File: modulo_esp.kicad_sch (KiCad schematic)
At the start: 0 parts

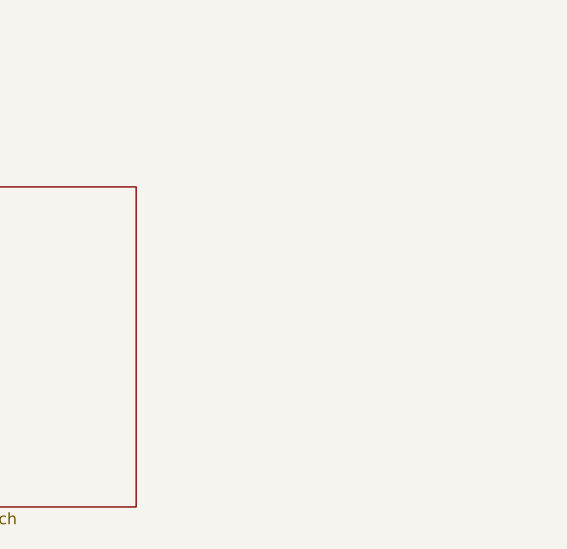
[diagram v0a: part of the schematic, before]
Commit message: Adicionado BG95-M3 e TVS do PHY Ethernet
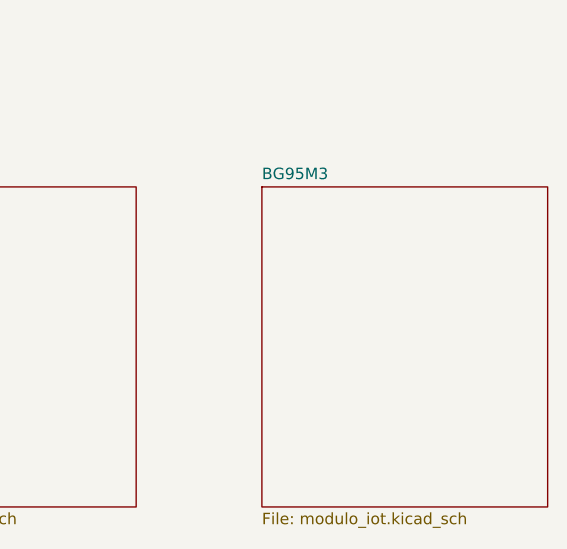
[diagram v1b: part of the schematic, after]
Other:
- added sheet BG95M3 (modulo_iot.kicad_sch)
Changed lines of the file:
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@@
+    )
+  )
+  (sheet (at 144.78 100.33) (size 31.75 35.56) (fields_autoplaced)
+    (stroke (width 0.1524) (type solid) (color 0 0 0 0))
+    (fill (color 0 0 0 0.0000))
+    (property "Sheet name" "BG95M3" (id 0) (at 144.78 99.6184 0)
+      (effects (font (size 1.27 1.27)) (justify left bottom))
+    )
+    (property "Sheet file" "modulo_iot.kicad_sch" (id 1) (at 144.78 136.4746 0)
+      (effects (font (size 1.27 1.27)) (justify left top))
     )
   )
@@
     (path "/7b11f4fb-9ca5-474d-979f-5c95c69d797c" (page "3"))
     (path "/fad468d2-9036-4024-8b69-088056b4a2a2" (page "4"))
+    (path "/42a2b2c3-5ebb-49d9-aedb-3a59eff4693b" (page "5"))
   )
   (symbol_instances
@@
       (reference "#PWR061") (unit 1) (value "GNDREF") (footprint "")
     )
+    (path "/42a2b2c3-5ebb-49d9-aedb-3a59eff4693b/17eac0f3-7baf-4b59-a491-3c654eaf5fe4"
+      (reference "#PWR?") (unit 1) (value "+3.3V") (footprint "")
+    )
+    (path "/42a2b2c3-5ebb-49d9-aedb-3a59eff4693b/60039f13-a1c0-40c4-8050-5e51646e9a0d"
+      (reference "#PWR?") (unit 1) (value "GNDREF") (footprint "")
+    )
     (path "/32e232d5-57bb-46e3-a8e5-df7ec6f170f8/4963f019-3ead-4e93-94b8-58e03e90d2e2"
       (reference "C1") (unit 1) (value "10nF") (footprint "Capacitor_SMD:C_0402_1005Metric_Pad0.74x0.62mm_HandSolder")
@@
       (reference "C32") (unit 1) (value "100nF/16V") (footprint "Capacitor_SMD:C_0402_1005Metric_Pad0.74x0.62mm_HandSolder")
     )
+    (path "/42a2b2c3-5ebb-49d9-aedb-3a59eff4693b/6ed173b9-0107-444a-98f2-2260e0361c0d"
+      (reference "C?") (unit 1) (value "10pF/16V") (footprint "Capacitor_SMD:C_0402_1005Metric_Pad0.74x0.62mm_HandSolder")
+    )
+    (path "/42a2b2c3-5ebb-49d9-aedb-3a59eff4693b/7ff4c112-8fbe-4ecb-a0b4-8ca060998c53"
+      (reference "C?") (unit 1) (value "100nF/16V") (footprint "Capacitor_SMD:C_0402_1005Metric_Pad0.74x0.62mm_HandSolder")
+    )
+    (path "/42a2b2c3-5ebb-49d9-aedb-3a59eff4693b/ddaca210-6aa5-4586-98c1-7d892363a5ca"
+      (reference "C?") (unit 1) (value "33pF/16V") (footprint "Capacitor_SMD:C_0402_1005Metric_Pad0.74x0.62mm_HandSolder")
+    )
     (path "/32e232d5-57bb-46e3-a8e5-df7ec6f170f8/ba36ba6b-a53c-4362-97a0-ed858cd67a0d"
       (reference "CON1") (unit 1) (value "USB_B_Micro") (footprint "Connector_USB:USB_Micro-B_GCT_USB3076-30-A")
@@
       (reference "D4") (unit 1) (value "LED_GREEN") (footprint "LED_SMD:LED_0603_1608Metric_Pad1.05x0.95mm_HandSolder")
     )
+    (path "/7b11f4fb-9ca5-474d-979f-5c95c69d797c/0f67a77a-a6d0-4ea2-83c0-566b7b3a544d"
+      (reference "D?") (unit 1) (value "SP4020-01FTG-C") (footprint "Diode_SMD:D_SOD-323_HandSoldering")
+    )
+    (path "/7b11f4fb-9ca5-474d-979f-5c95c69d797c/d2017409-fbbf-4cef-a069-85452552d341"
+      (reference "D?") (unit 1) (value "SP4020-01FTG-C") (footprint "Diode_SMD:D_SOD-323_HandSoldering")
+    )
     (path "/7b11f4fb-9ca5-474d-979f-5c95c69d797c/5f06ff99-4823-4432-98ba-354afdb4edf1"
       (reference "J1") (unit 1) (value "8P8C") (footprint "Connector_RJ:RJ45_OST_PJ012-8P8CX_Vertical")
@@
     )
     (path "/7b11f4fb-9ca5-474d-979f-5c95c69d797c/951fddfb-1e9f-41f6-bed8-d1a8ad2d6e7e"
-      (reference "TR1") (unit 1) (value "Wuerth_749013011A") (footprint "Transformer_SMD:Transformer_Ethernet_Wuerth_749013011A")
+      (reference "TR1") (unit 1) (value "S16A-1102") (footprint "Transformer_SMD:Transformer_Ethernet_Wuerth_749013011A")
     )
     (path "/32e232d5-57bb-46e3-a8e5-df7ec6f170f8/a28f0fc0-0b1e-4a63-985f-c627cc83cd03"
@@
       (reference "U4") (unit 1) (value "ESP32-WROOM-32D") (footprint "RF_Module:ESP32-WROOM-32")
     )
+    (path "/42a2b2c3-5ebb-49d9-aedb-3a59eff4693b/be32796f-5b67-4447-8899-f2a301939123"
+      (reference "U?") (unit 1) (value "BG95-M3") (footprint "BG95:XCVR_BG95")
+    )
     (path "/7b11f4fb-9ca5-474d-979f-5c95c69d797c/edc90c5f-8130-4162-bf12-0f0546719f39"

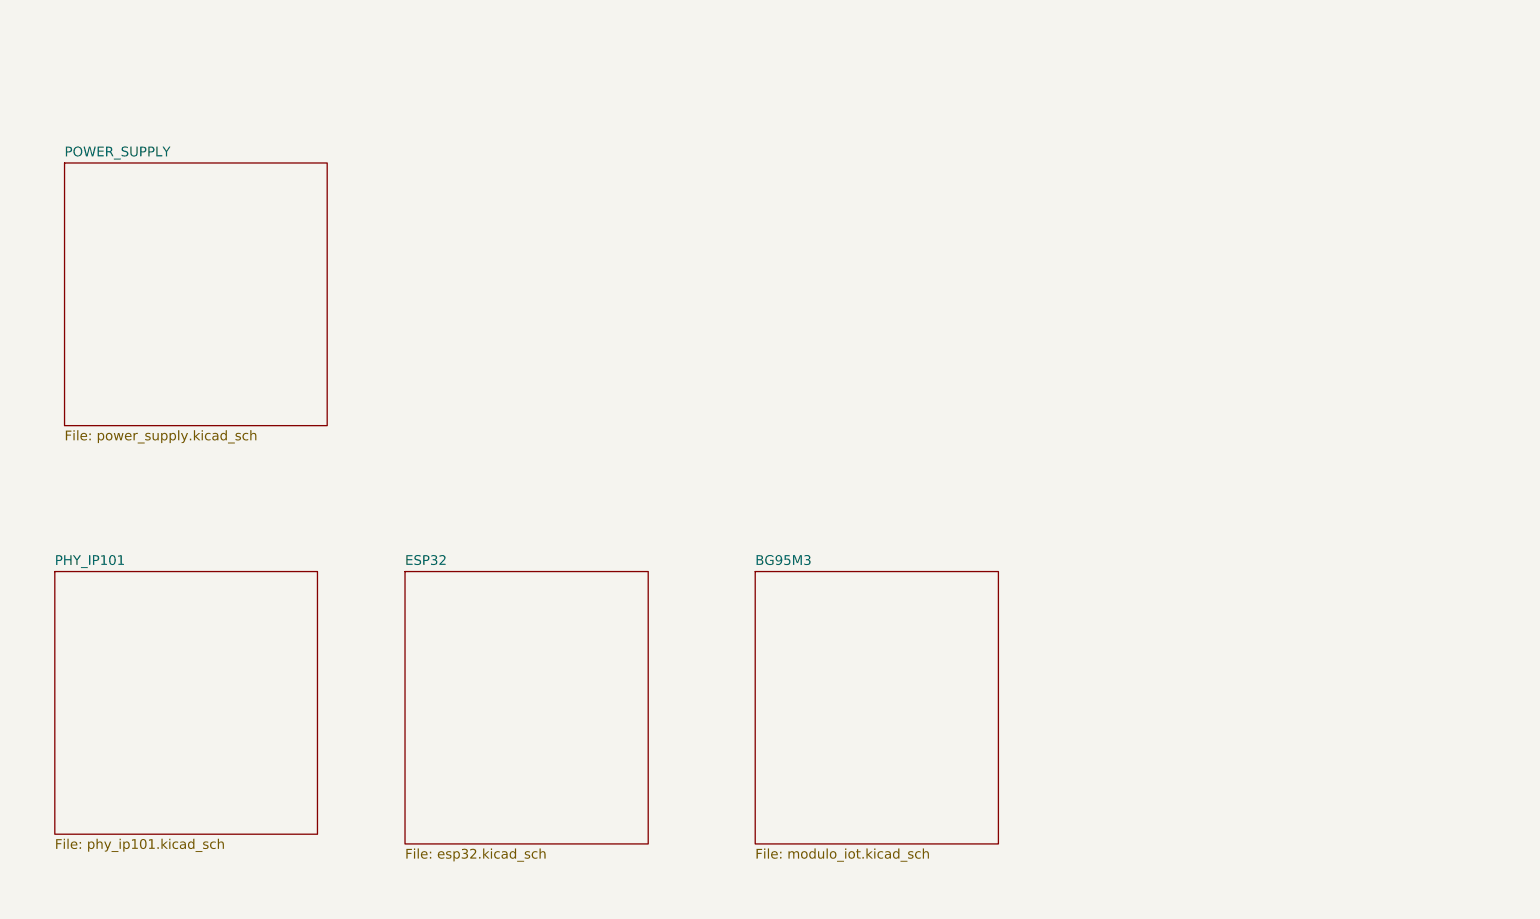
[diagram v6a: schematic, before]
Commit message: Adicionado hierarchical label
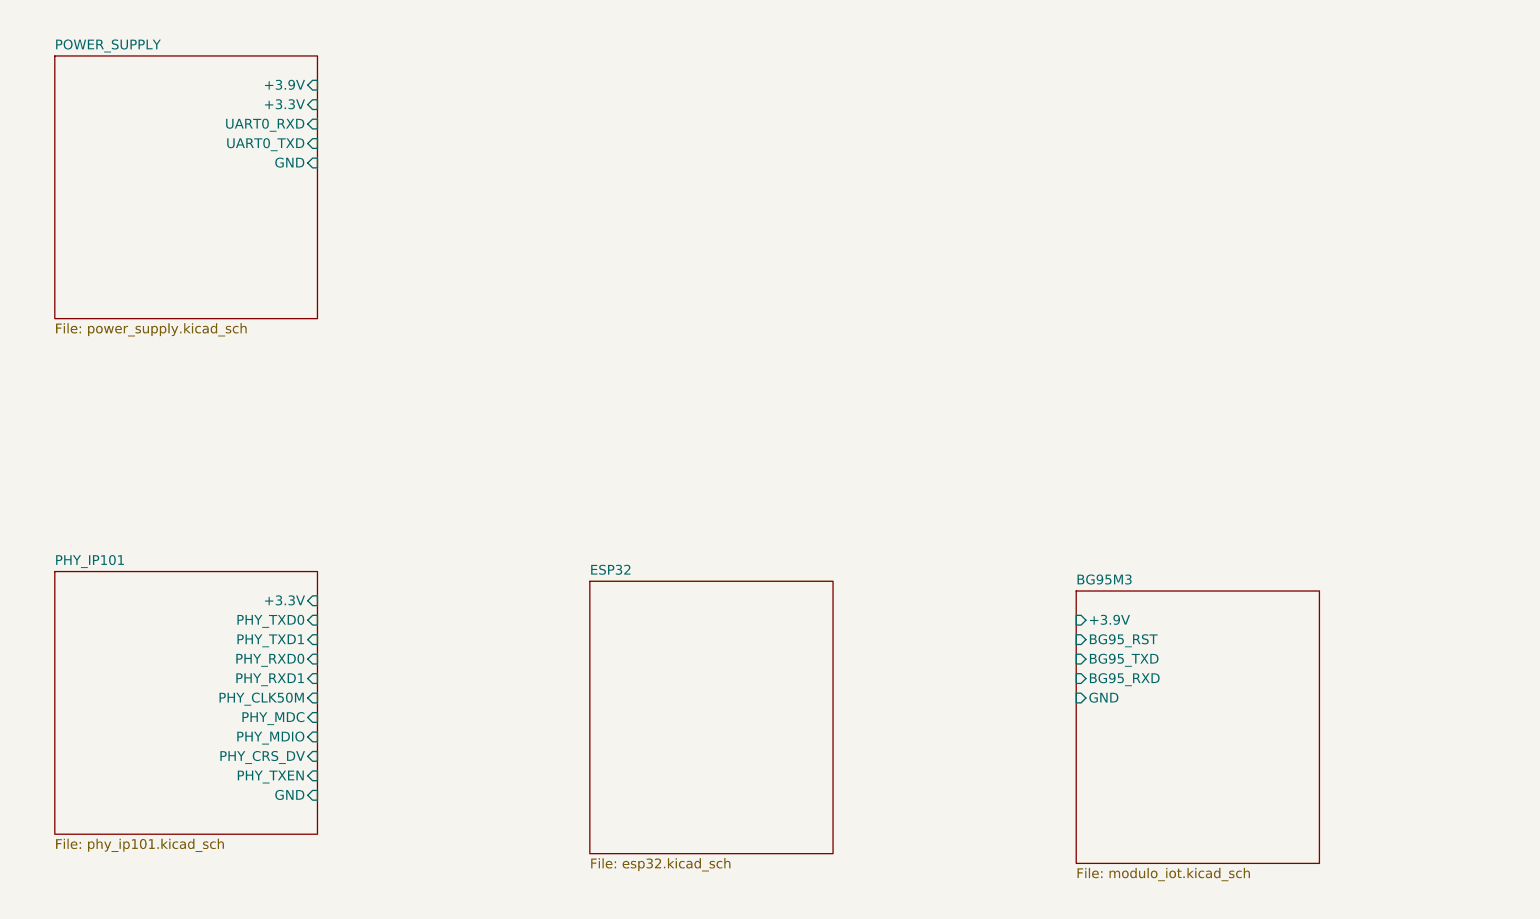
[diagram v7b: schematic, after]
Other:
- sheet BG95M3 ports: added +3.9V, BG95_RST, BG95_RXD, BG95_TXD, GND; removed none
- sheet PHY_IP101 ports: added +3.3V, GND, PHY_CLK50M, PHY_CRS_DV, PHY_MDC, PHY_MDIO, PHY_RXD0, PHY_RXD1, PHY_TXD0, PHY_TXD1, PHY_TXEN; removed none
- sheet POWER_SUPPLY ports: added +3.3V, +3.9V, GND, UART0_RXD, UART0_TXD; removed none
- company: ESP32-WROOM -> Magalhaes

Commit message: Cont. hierarchical label e descrição das folhas
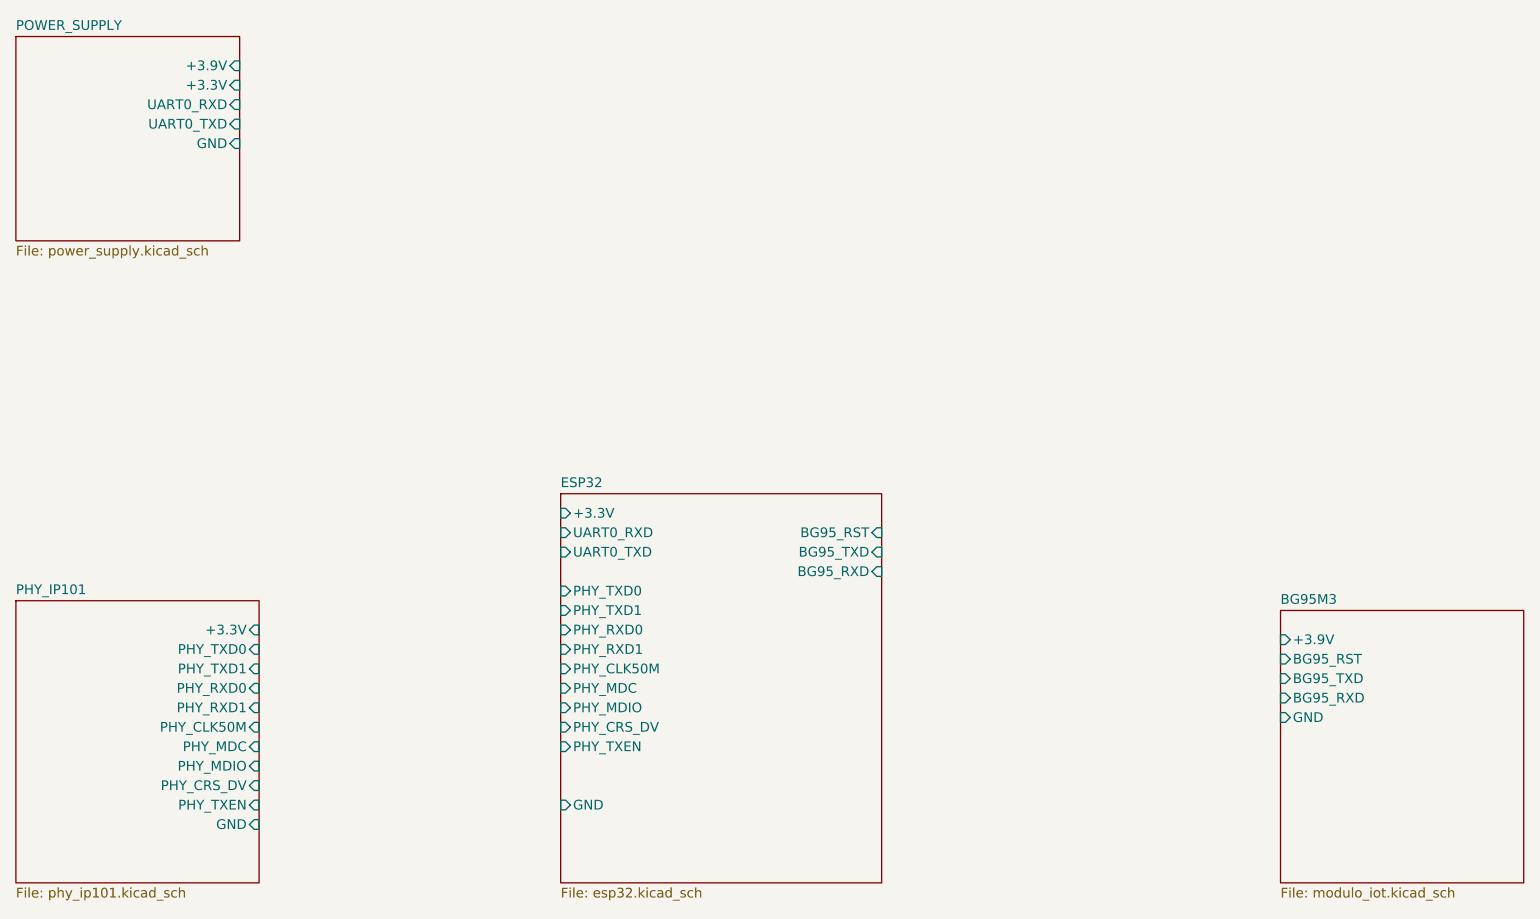
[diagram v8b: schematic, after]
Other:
- sheet ESP32 ports: added +3.3V, BG95_RST, BG95_RXD, BG95_TXD, GND, PHY_CLK50M, PHY_CRS_DV, PHY_MDC, PHY_MDIO, PHY_RXD0, PHY_RXD1, PHY_TXD0, PHY_TXD1, PHY_TXEN, UART0_RXD, UART0_TXD; removed none
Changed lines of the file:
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@@
     (comment 2 "Variant 1: Full")
   )
-  (sheet (at 53.34 33.02) (size 34.29 34.29) (fields_autoplaced)
+  (sheet (at 48.26 30.48) (size 29.21 26.67) (fields_autoplaced)
     (stroke (width 0.1524) (type solid) (color 0 0 0 0))
     (fill (color 0 0 0 0.0000))
-    (property "Sheet name" "POWER_SUPPLY" (id 0) (at 53.34 32.3084 0)
+    (property "Sheet name" "POWER_SUPPLY" (id 0) (at 48.26 29.7684 0)
       (effects (font (size 1.27 1.27)) (justify left bottom))
     )
-    (property "Sheet file" "power_supply.kicad_sch" (id 1) (at 53.34 67.8946 0)
+    (property "Sheet file" "power_supply.kicad_sch" (id 1) (at 48.26 57.7346 0)
       (effects (font (size 1.27 1.27)) (justify left top))
     )
-    (pin "+3.9V" input (at 87.63 36.83 0)
+    (pin "+3.9V" input (at 77.47 34.29 0)
       (effects (font (size 1.27 1.27)) (justify right))
     )
-    (pin "+3.3V" input (at 87.63 39.37 0)
+    (pin "+3.3V" input (at 77.47 36.83 0)
       (effects (font (size 1.27 1.27)) (justify right))
     )
-    (pin "UART0_RXD" input (at 87.63 41.91 0)
+    (pin "UART0_RXD" input (at 77.47 39.37 0)
       (effects (font (size 1.27 1.27)) (justify right))
     )
-    (pin "UART0_TXD" input (at 87.63 44.45 0)
+    (pin "UART0_TXD" input (at 77.47 41.91 0)
       (effects (font (size 1.27 1.27)) (justify right))
     )
-    (pin "GND" input (at 87.63 46.99 0)
+    (pin "GND" input (at 77.47 44.45 0)
       (effects (font (size 1.27 1.27)) (justify right))
     )
   )
-  (sheet (at 186.69 102.87) (size 31.75 35.56) (fields_autoplaced)
+  (sheet (at 213.36 105.41) (size 31.75 35.56) (fields_autoplaced)
     (stroke (width 0.1524) (type solid) (color 0 0 0 0))
     (fill (color 0 0 0 0.0000))
-    (property "Sheet name" "BG95M3" (id 0) (at 186.69 102.1584 0)
+    (property "Sheet name" "BG95M3" (id 0) (at 213.36 104.6984 0)
       (effects (font (size 1.27 1.27)) (justify left bottom))
     )
-    (property "Sheet file" "modulo_iot.kicad_sch" (id 1) (at 186.69 139.0146 0)
+    (property "Sheet file" "modulo_iot.kicad_sch" (id 1) (at 213.36 141.5546 0)
       (effects (font (size 1.27 1.27)) (justify left top))
     )
-    (pin "BG95_RST" input (at 186.69 109.22 180)
+    (pin "BG95_RST" input (at 213.36 111.76 180)
       (effects (font (size 1.27 1.27)) (justify left))
     )
-    (pin "BG95_TXD" input (at 186.69 111.76 180)
+    (pin "BG95_TXD" input (at 213.36 114.3 180)
       (effects (font (size 1.27 1.27)) (justify left))
     )
-    (pin "BG95_RXD" input (at 186.69 114.3 180)
+    (pin "BG95_RXD" input (at 213.36 116.84 180)
       (effects (font (size 1.27 1.27)) (justify left))
     )
-    (pin "+3.9V" input (at 186.69 106.68 180)
+    (pin "+3.9V" input (at 213.36 109.22 180)
       (effects (font (size 1.27 1.27)) (justify left))
     )
-    (pin "GND" input (at 186.69 116.84 180)
+    (pin "GND" input (at 213.36 119.38 180)
       (effects (font (size 1.27 1.27)) (justify left))
     )
   )
-  (sheet (at 53.34 100.33) (size 34.29 34.29) (fields_autoplaced)
+  (sheet (at 48.26 104.14) (size 31.75 36.83) (fields_autoplaced)
     (stroke (width 0.1524) (type solid) (color 0 0 0 0))
     (fill (color 0 0 0 0.0000))
-    (property "Sheet name" "PHY_IP101" (id 0) (at 53.34 99.6184 0)
+    (property "Sheet name" "PHY_IP101" (id 0) (at 48.26 103.4284 0)
       (effects (font (size 1.27 1.27)) (justify left bottom))
     )
-    (property "Sheet file" "phy_ip101.kicad_sch" (id 1) (at 53.34 135.2046 0)
+    (property "Sheet file" "phy_ip101.kicad_sch" (id 1) (at 48.26 141.5546 0)
       (effects (font (size 1.27 1.27)) (justify left top))
     )
-    (pin "+3.3V" input (at 87.63 104.14 0)
+    (pin "+3.3V" input (at 80.01 107.95 0)
       (effects (font (size 1.27 1.27)) (justify right))
     )
-    (pin "GND" input (at 87.63 129.54 0)
+    (pin "GND" input (at 80.01 133.35 0)
       (effects (font (size 1.27 1.27)) (justify right))
     )
-    (pin "PHY_TXD1" input (at 87.63 109.22 0)
+    (pin "PHY_TXD1" input (at 80.01 113.03 0)
       (effects (font (size 1.27 1.27)) (justify right))
     )
-    (pin "PHY_CRS_DV" input (at 87.63 124.46 0)
+    (pin "PHY_CRS_DV" input (at 80.01 128.27 0)
       (effects (font (size 1.27 1.27)) (justify right))
     )
-    (pin "PHY_RXD0" input (at 87.63 111.76 0)
+    (pin "PHY_RXD0" input (at 80.01 115.57 0)
       (effects (font (size 1.27 1.27)) (justify right))
     )
-    (pin "PHY_TXD0" input (at 87.63 106.68 0)
+    (pin "PHY_TXD0" input (at 80.01 110.49 0)
       (effects (font (size 1.27 1.27)) (justify right))
     )
-    (pin "PHY_RXD1" input (at 87.63 114.3 0)
+    (pin "PHY_RXD1" input (at 80.01 118.11 0)
       (effects (font (size 1.27 1.27)) (justify right))
     )
-    (pin "PHY_CLK50M" input (at 87.63 116.84 0)
+    (pin "PHY_CLK50M" input (at 80.01 120.65 0)
       (effects (font (size 1.27 1.27)) (justify right))
     )
-    (pin "PHY_MDC" input (at 87.63 119.38 0)
+    (pin "PHY_MDC" input (at 80.01 123.19 0)
       (effects (font (size 1.27 1.27)) (justify right))
     )
-    (pin "PHY_MDIO" input (at 87.63 121.92 0)
+    (pin "PHY_MDIO" input (at 80.01 125.73 0)
       (effects (font (size 1.27 1.27)) (justify right))
     )
-    (pin "PHY_TXEN" input (at 87.63 127 0)
+    (pin "PHY_TXEN" input (at 80.01 130.81 0)
       (effects (font (size 1.27 1.27)) (justify right))
     )
   )
-  (sheet (at 123.19 101.6) (size 31.75 35.56) (fields_autoplaced)
+  (sheet (at 119.38 90.17) (size 41.91 50.8) (fields_autoplaced)
     (stroke (width 0.1524) (type solid) (color 0 0 0 0))
     (fill (color 0 0 0 0.0000))
-    (property "Sheet name" "ESP32" (id 0) (at 123.19 100.8884 0)
+    (property "Sheet name" "ESP32" (id 0) (at 119.38 89.4584 0)
       (effects (font (size 1.27 1.27)) (justify left bottom))
     )
-    (property "Sheet file" "esp32.kicad_sch" (id 1) (at 123.19 137.7446 0)
+    (property "Sheet file" "esp32.kicad_sch" (id 1) (at 119.38 141.5546 0)
       (effects (font (size 1.27 1.27)) (justify left top))
     )
+    (pin "BG95_RXD" input (at 161.29 100.33 0)
+      (effects (font (size 1.27 1.27)) (justify right))
+    )
+    (pin "BG95_TXD" input (at 161.29 97.79 0)
+      (effects (font (size 1.27 1.27)) (justify right))
+    )
+    (pin "BG95_RST" input (at 161.29 95.25 0)
+      (effects (font (size 1.27 1.27)) (justify right))
+    )
+    (pin "UART0_RXD" input (at 119.38 95.25 180)
+      (effects (font (size 1.27 1.27)) (justify left))
+    )
+    (pin "UART0_TXD" input (at 119.38 97.79 180)
+      (effects (font (size 1.27 1.27)) (justify left))
+    )
+    (pin "+3.3V" input (at 119.38 92.71 180)
+      (effects (font (size 1.27 1.27)) (justify left))
+    )
+    (pin "GND" input (at 119.38 130.81 180)
+      (effects (font (size 1.27 1.27)) (justify left))
+    )
+    (pin "PHY_TXEN" input (at 119.38 123.19 180)
+      (effects (font (size 1.27 1.27)) (justify left))
+    )
+    (pin "PHY_MDIO" input (at 119.38 118.11 180)
+      (effects (font (size 1.27 1.27)) (justify left))
+    )
+    (pin "PHY_CRS_DV" input (at 119.38 120.65 180)
+      (effects (font (size 1.27 1.27)) (justify left))
+    )
+    (pin "PHY_CLK50M" input (at 119.38 113.03 180)
+      (effects (font (size 1.27 1.27)) (justify left))
+    )
+    (pin "PHY_RXD1" input (at 119.38 110.49 180)
+      (effects (font (size 1.27 1.27)) (justify left))
+    )
+    (pin "PHY_MDC" input (at 119.38 115.57 180)
+      (effects (font (size 1.27 1.27)) (justify left))
+    )
+    (pin "PHY_RXD0" input (at 119.38 107.95 180)
+      (effects (font (size 1.27 1.27)) (justify left))
+    )
+    (pin "PHY_TXD0" input (at 119.38 102.87 180)
+      (effects (font (size 1.27 1.27)) (justify left))
+    )
+    (pin "PHY_TXD1" input (at 119.38 105.41 180)
+      (effects (font (size 1.27 1.27)) (justify left))
+    )
   )
